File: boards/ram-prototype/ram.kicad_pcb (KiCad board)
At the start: 4 copper layers, 158 x 90 mm, 391 parts, among them J1 PinHeader_1x16_P2.54mm_Vertic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, U1 DSBGA\-5_NumericPads, U10 DSBGA\-5_NumericPads, U100 DSBGA\-5_NumericPads, U101 DSBGA\-5_NumericPads, U102 DSBGA\-5_NumericPads, U103 DSBGA\-5_NumericPads, U104 DSBGA\-5_NumericPads, U105 DSBGA\-5_NumericPads, U106 DSBGA\-5_NumericPads, U107 DSBGA\-5_NumericPads, U108 DSBGA\-5_NumericPads, U109 DSBGA\-5_NumericPads, U11 DSBGA\-5_NumericPads, U110 DSBGA\-5_NumericPads, U111 DSBGA\-5_NumericPads, U112 DSBGA\-5_NumericPads, U113 DSBGA\-5_NumericPads, U114 DSBGA\-5_NumericPads, U115 DSBGA\-5_NumericPads, U116 DSBGA\-5_NumericPads, U117 DSBGA\-5_NumericPads, U118 DSBGA\-5_NumericPads, U119 DSBGA\-5_NumericPads, U12 DSBGA\-5_NumericPads, U120 DSBGA\-5_NumericPads, U121 DSBGA\-5_NumericPads, U122 DSBGA\-5_NumericPads, U123 DSBGA\-5_NumericPads, U124 DSBGA\-5_NumericPads, U125 DSBGA\-5_NumericPads, U126 DSBGA\-5_NumericPads, U127 DSBGA\-5_NumericPads, U128 DSBGA\-5_NumericPads, U129 DSBGA\-5_NumericPads, U13 DSBGA\-5_NumericPads, U130 DSBGA\-5_NumericPads, U131 DSBGA\-5_NumericPads, U132 DSBGA\-5_NumericPads, U133 DSBGA\-5_NumericPads, U134 DSBGA\-5_NumericPads, U135 DSBGA\-5_NumericPads, U136 DSBGA\-5_NumericPads, U137 DSBGA\-5_NumericPads, U138 DSBGA\-5_NumericPads, U139 DSBGA\-5_NumericPads, U14 DSBGA\-5_NumericPads, U140 DSBGA\-5_NumericPads, U141 DSBGA\-5_NumericPads, U142 DSBGA\-5_NumericPads, U143 DSBGA\-5_NumericPads, U144 DSBGA\-5_NumericPads, U145 DSBGA\-5_NumericPads, U146 DSBGA\-5_NumericPads, U147 DSBGA\-5_NumericPads, U148 DSBGA\-5_NumericPads, U149 DSBGA\-5_NumericPads, U15 DSBGA\-5_NumericPads, U150 DSBGA\-5_NumericPads, U151 DSBGA\-5_NumericPads, U152 DSBGA\-5_NumericPads, U153 DSBGA\-5_NumericPads, U154 DSBGA\-5_NumericPads, U155 DSBGA\-5_NumericPads, U156 DSBGA\-5_NumericPads, U157 DSBGA\-5_NumericPads, U158 DSBGA\-5_NumericPads, U16 DSBGA\-5_NumericPads, U17 DSBGA\-5_NumericPads, U18 DSBGA\-5_NumericPads, U19 DSBGA\-5_NumericPads, U2 DSBGA\-5_NumericPads, U20 DSBGA\-5_NumericPads, U21 DSBGA\-5_NumericPads, U22 DSBGA\-5_NumericPads, U23 DSBGA\-8_NumericPads, U24 DSBGA\-8_NumericPads, U25 DSBGA\-8_NumericPads, U26 DSBGA\-8_NumericPads, U27 DSBGA\-8_NumericPads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

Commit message: Change layout
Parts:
- moved D35 48.6 mm to (73.3, 28.0)
- moved R35 48.6 mm to (73.3, 28.0)
- moved U21 48.6 mm to (70.9, 28.0)
- moved D34 46.7 mm to (73.3, 24.0)
- moved R34 46.7 mm to (73.3, 24.0)
- moved U20 46.7 mm to (70.9, 24.0)
- moved D33 45.7 mm to (73.3, 20.0)
- moved R33 45.7 mm to (73.3, 20.0)
- moved U19 45.7 mm to (70.9, 20.0)
- moved D36 40.0 mm to (73.3, 32.0)
- moved R36 40.0 mm to (73.3, 32.0)
- moved U22 40.0 mm to (70.9, 32.0)
- moved D31 39.2 mm to (62.4, 28.0)
- moved R31 39.2 mm to (62.4, 28.0)
- moved U17 39.2 mm to (60.0, 28.0)
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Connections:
- D1 pad 2: /Address Decoder/A0 -> /Control Logic/nOE
- D10 pad 2: /D3 -> /D4
- D11 pad 2: /D4 -> /D5
- D12 pad 2: /D5 -> /D6
- D13 pad 2: /D6 -> /D7
- D14 pad 2: /D7 -> /Column Select/A2
- D2 pad 2: /Address Decoder/A1 -> /Control Logic/nWE
- D3 pad 2: /Column Select/A2 -> /Control Logic/nCE
- D4 pad 2: /Control Logic/nOE -> /Address Decoder/A1
- D5 pad 2: /Control Logic/nWE -> /Address Decoder/A0
- D6 pad 2: /Control Logic/nCE -> /D0
- D7 pad 2: /D0 -> /D1
- D8 pad 2: /D1 -> /D2
- D9 pad 2: /D2 -> /D3
- J1 pad 10: /Control Logic/nCE -> /D0
- J1 pad 11: /Control Logic/nWE -> /Address Decoder/A0
- J1 pad 12: /Control Logic/nOE -> /Address Decoder/A1
- J1 pad 13: /Column Select/A2 -> /Control Logic/nCE
- J1 pad 14: /Address Decoder/A1 -> /Control Logic/nWE
- J1 pad 15: /Address Decoder/A0 -> /Control Logic/nOE
- J1 pad 2: /D7 -> /Column Select/A2
- J1 pad 3: /D6 -> /D7
- J1 pad 4: /D5 -> /D6
- J1 pad 5: /D4 -> /D5
- J1 pad 6: /D3 -> /D4
- J1 pad 7: /D2 -> /D3
- J1 pad 8: /D1 -> /D2
- J1 pad 9: /D0 -> /D1
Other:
- board size 158 x 90 mm -> 164 x 98 mm

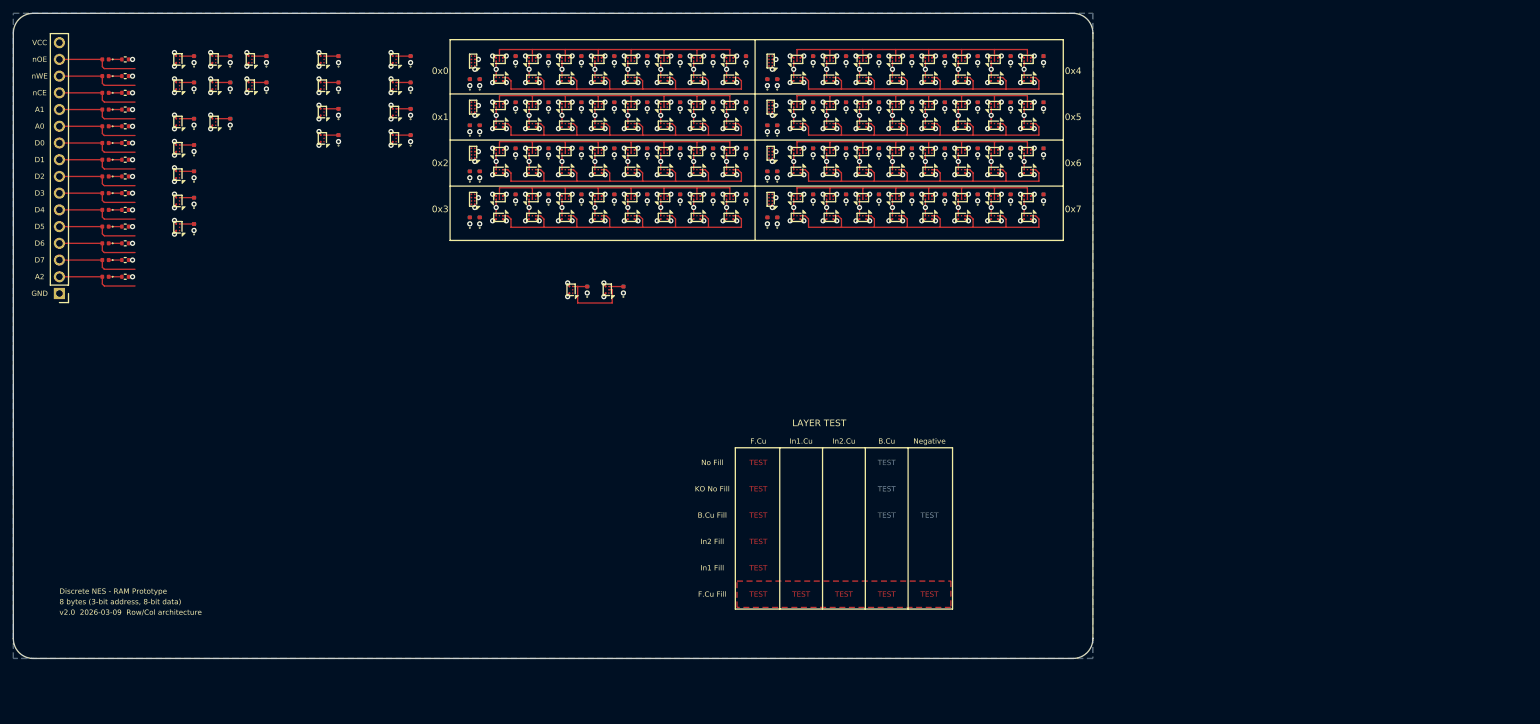
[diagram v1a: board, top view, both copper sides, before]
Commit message: clean up silkscreen
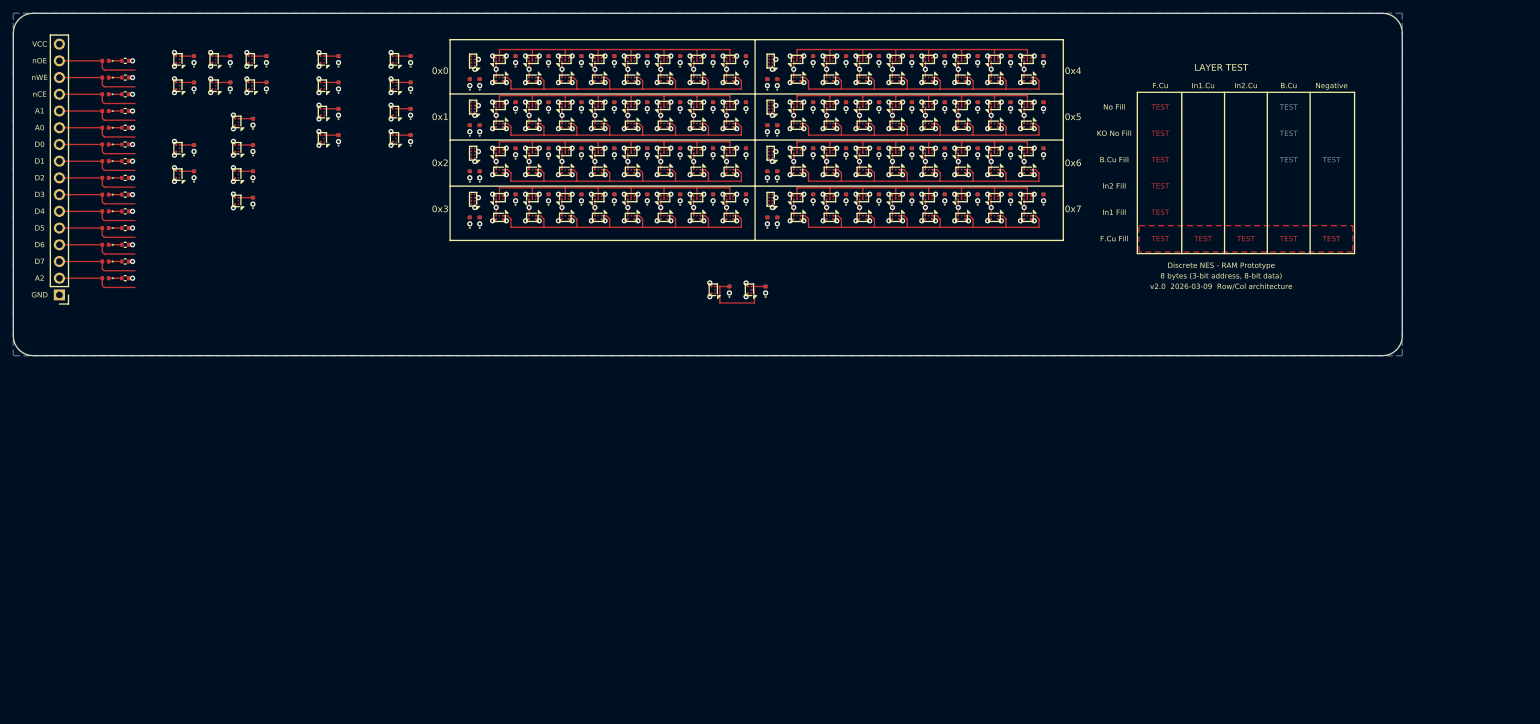
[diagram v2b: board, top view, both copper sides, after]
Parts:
- moved D21 21.6 mm to (121.8, 55.0)
- moved D22 21.6 mm to (127.3, 55.0)
- moved R21 21.6 mm to (121.8, 55.0)
- moved R22 21.6 mm to (127.3, 55.0)
- moved U7 21.6 mm to (119.3, 55.0)
- moved U8 21.6 mm to (124.8, 55.0)
- moved U3 9.80 mm to (47.0, 29.5)
- moved U4 9.80 mm to (47.0, 33.5)
- moved U5 9.80 mm to (47.0, 37.5)
- moved U6 9.80 mm to (47.0, 41.5)
- moved D17 9.80 mm to (49.4, 29.5)
- moved D18 9.80 mm to (49.4, 33.5)
- moved D19 9.80 mm to (49.4, 37.5)
- moved D20 9.80 mm to (49.4, 41.5)
- moved R17 9.80 mm to (49.4, 29.5)
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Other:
- board size 164 x 98 mm -> 211 x 52 mm

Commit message: refactor read and write schematics into row control sheets
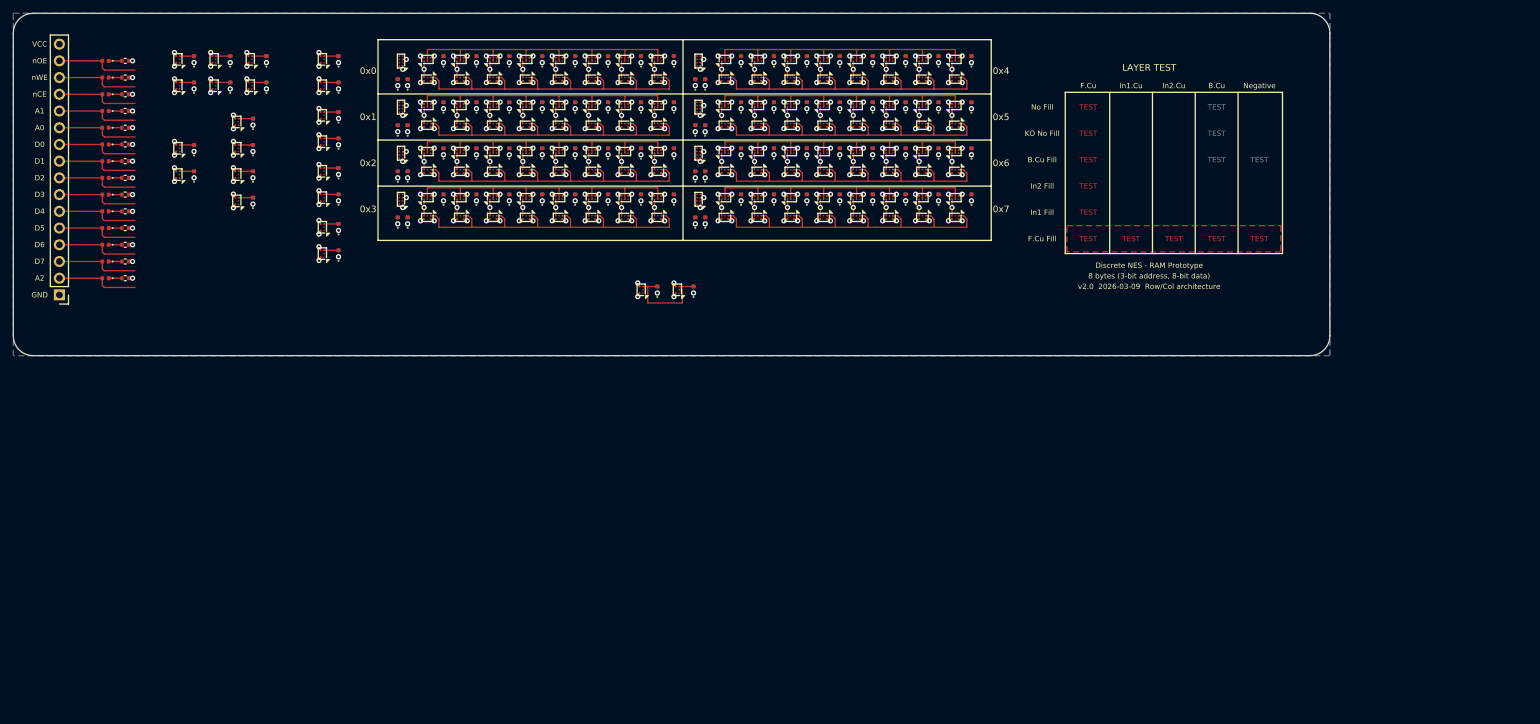
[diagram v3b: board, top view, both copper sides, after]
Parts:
- moved U22 20.6 mm to (60.0, 49.5)
- moved D36 20.6 mm to (62.4, 49.5)
- moved R36 20.6 mm to (62.4, 49.5)
- moved U21 17.0 mm to (60.0, 41.0)
- moved D35 17.0 mm to (62.4, 41.0)
- moved R35 17.0 mm to (62.4, 41.0)
- moved U20 13.9 mm to (60.0, 32.5)
- moved D34 13.9 mm to (62.4, 32.5)
- moved R34 13.9 mm to (62.4, 32.5)
- moved D32 13.5 mm to (62.4, 45.5)
- moved R32 13.5 mm to (62.4, 45.5)
- moved U18 13.5 mm to (60.0, 45.5)
- moved U19 11.7 mm to (60.0, 24.0)
- moved D33 11.7 mm to (62.4, 24.0)
- moved R33 11.7 mm to (62.4, 24.0)
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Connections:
- net /Control Logic/READ_EN renamed /READ_EN
- net /Control Logic/WRITE_ACTIVE renamed /WRITE_ACTIVE
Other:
- board size 211 x 52 mm -> 200 x 52 mm

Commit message: Add initial changes to make logic close to final
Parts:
- added D117: LED_0402_1005Metric, LED_SMD:LED_0402_1005Metric, F.Cu at (103.3, 27.0)
- added D118: LED_0402_1005Metric, LED_SMD:LED_0402_1005Metric, F.Cu at (103.3, 34.0)
- added D119: LED_0402_1005Metric, LED_SMD:LED_0402_1005Metric, F.Cu at (103.3, 41.0)
- added D120: LED_0402_1005Metric, LED_SMD:LED_0402_1005Metric, F.Cu at (148.6, 20.0)
- added D121: LED_0402_1005Metric, LED_SMD:LED_0402_1005Metric, F.Cu at (148.6, 27.0)
- added D122: LED_0402_1005Metric, LED_SMD:LED_0402_1005Metric, F.Cu at (148.6, 34.0)
- added D123: LED_0402_1005Metric, LED_SMD:LED_0402_1005Metric, F.Cu at (148.6, 41.0)
- added D124: LED_0402_1005Metric, LED_SMD:LED_0402_1005Metric, F.Cu at (98.3, 20.0)
- added D125: LED_0402_1005Metric, LED_SMD:LED_0402_1005Metric, F.Cu at (98.3, 27.0)
- added D126: LED_0402_1005Metric, LED_SMD:LED_0402_1005Metric, F.Cu at (98.3, 34.0)
- added D127: LED_0402_1005Metric, LED_SMD:LED_0402_1005Metric, F.Cu at (98.3, 41.0)
- added D128: LED_0402_1005Metric, LED_SMD:LED_0402_1005Metric, F.Cu at (143.6, 20.0)
- added D129: LED_0402_1005Metric, LED_SMD:LED_0402_1005Metric, F.Cu at (143.6, 27.0)
- added D130: LED_0402_1005Metric, LED_SMD:LED_0402_1005Metric, F.Cu at (143.6, 34.0)
- added D131: LED_0402_1005Metric, LED_SMD:LED_0402_1005Metric, F.Cu at (143.6, 41.0)
- added D132: LED_0402_1005Metric, LED_SMD:LED_0402_1005Metric, F.Cu at (93.3, 20.0)
- added D133: LED_0402_1005Metric, LED_SMD:LED_0402_1005Metric, F.Cu at (93.3, 27.0)
- added D134: LED_0402_1005Metric, LED_SMD:LED_0402_1005Metric, F.Cu at (93.3, 34.0)
- added D135: LED_0402_1005Metric, LED_SMD:LED_0402_1005Metric, F.Cu at (93.3, 41.0)
- added D136: LED_0402_1005Metric, LED_SMD:LED_0402_1005Metric, F.Cu at (138.6, 20.0)
- added D137: LED_0402_1005Metric, LED_SMD:LED_0402_1005Metric, F.Cu at (138.6, 27.0)
- added D138: LED_0402_1005Metric, LED_SMD:LED_0402_1005Metric, F.Cu at (138.6, 34.0)
- added D139: LED_0402_1005Metric, LED_SMD:LED_0402_1005Metric, F.Cu at (138.6, 41.0)
- added D140: LED_0402_1005Metric, LED_SMD:LED_0402_1005Metric, F.Cu at (88.3, 20.0)
- added D141: LED_0402_1005Metric, LED_SMD:LED_0402_1005Metric, F.Cu at (88.3, 27.0)
- added D142: LED_0402_1005Metric, LED_SMD:LED_0402_1005Metric, F.Cu at (88.3, 34.0)
- added D143: LED_0402_1005Metric, LED_SMD:LED_0402_1005Metric, F.Cu at (88.3, 41.0)
- added D144: LED_0402_1005Metric, LED_SMD:LED_0402_1005Metric, F.Cu at (133.6, 20.0)
- added D145: LED_0402_1005Metric, LED_SMD:LED_0402_1005Metric, F.Cu at (133.6, 27.0)
- added D146: LED_0402_1005Metric, LED_SMD:LED_0402_1005Metric, F.Cu at (133.6, 34.0)
- added D147: LED_0402_1005Metric, LED_SMD:LED_0402_1005Metric, F.Cu at (133.6, 41.0)
- added D148: LED_0402_1005Metric, LED_SMD:LED_0402_1005Metric, F.Cu at (83.3, 20.0)
- added D149: LED_0402_1005Metric, LED_SMD:LED_0402_1005Metric, F.Cu at (83.3, 27.0)
- added D150: LED_0402_1005Metric, LED_SMD:LED_0402_1005Metric, F.Cu at (83.3, 34.0)
- added D151: LED_0402_1005Metric, LED_SMD:LED_0402_1005Metric, F.Cu at (83.3, 41.0)
- added D152: LED_0402_1005Metric, LED_SMD:LED_0402_1005Metric, F.Cu at (128.6, 20.0)
- added D153: LED_0402_1005Metric, LED_SMD:LED_0402_1005Metric, F.Cu at (128.6, 27.0)
- added D154: LED_0402_1005Metric, LED_SMD:LED_0402_1005Metric, F.Cu at (128.6, 34.0)
- added D155: LED_0402_1005Metric, LED_SMD:LED_0402_1005Metric, F.Cu at (128.6, 41.0)
- added D156: LED_0402_1005Metric, LED_SMD:LED_0402_1005Metric, F.Cu at (78.3, 20.0)
- added D157: LED_0402_1005Metric, LED_SMD:LED_0402_1005Metric, F.Cu at (78.3, 27.0)
- added D158: LED_0402_1005Metric, LED_SMD:LED_0402_1005Metric, F.Cu at (78.3, 34.0)
- added D159: LED_0402_1005Metric, LED_SMD:LED_0402_1005Metric, F.Cu at (78.3, 41.0)
- added D160: LED_0402_1005Metric, LED_SMD:LED_0402_1005Metric, F.Cu at (123.5, 20.0)
- added D161: LED_0402_1005Metric, LED_SMD:LED_0402_1005Metric, F.Cu at (123.5, 27.0)
- added D162: LED_0402_1005Metric, LED_SMD:LED_0402_1005Metric, F.Cu at (123.5, 34.0)
- added D163: LED_0402_1005Metric, LED_SMD:LED_0402_1005Metric, F.Cu at (123.5, 41.0)
- added J2: PinHeader_1x12_P2.54mm_Vertical, Connector_PinHeader_2.54mm:PinHeader_1x12_P2.54mm_Vertical, B.Cu at (38.0, 80.0)
- added J3: PinHeader_1x14_P2.54mm_Vertical, Connector_PinHeader_2.54mm:PinHeader_1x14_P2.54mm_Vertical, B.Cu at (165.3, 54.0)
- added R117: R_0402_1005Metric, Resistor_SMD:R_0402_1005Metric, B.Cu at (103.3, 27.0)
- added R118: R_0402_1005Metric, Resistor_SMD:R_0402_1005Metric, B.Cu at (103.3, 34.0)
- added R119: R_0402_1005Metric, Resistor_SMD:R_0402_1005Metric, B.Cu at (103.3, 41.0)
- added R120: R_0402_1005Metric, Resistor_SMD:R_0402_1005Metric, B.Cu at (148.6, 20.0)
- added R121: R_0402_1005Metric, Resistor_SMD:R_0402_1005Metric, B.Cu at (148.6, 27.0)
- added R122: R_0402_1005Metric, Resistor_SMD:R_0402_1005Metric, B.Cu at (148.6, 34.0)
- added R123: R_0402_1005Metric, Resistor_SMD:R_0402_1005Metric, B.Cu at (148.6, 41.0)
- added R124: R_0402_1005Metric, Resistor_SMD:R_0402_1005Metric, B.Cu at (98.3, 20.0)
- added R125: R_0402_1005Metric, Resistor_SMD:R_0402_1005Metric, B.Cu at (98.3, 27.0)
- added R126: R_0402_1005Metric, Resistor_SMD:R_0402_1005Metric, B.Cu at (98.3, 34.0)
- added R127: R_0402_1005Metric, Resistor_SMD:R_0402_1005Metric, B.Cu at (98.3, 41.0)
- added R128: R_0402_1005Metric, Resistor_SMD:R_0402_1005Metric, B.Cu at (143.6, 20.0)
- added R129: R_0402_1005Metric, Resistor_SMD:R_0402_1005Metric, B.Cu at (143.6, 27.0)
- added R130: R_0402_1005Metric, Resistor_SMD:R_0402_1005Metric, B.Cu at (143.6, 34.0)
- added R131: R_0402_1005Metric, Resistor_SMD:R_0402_1005Metric, B.Cu at (143.6, 41.0)
- added R132: R_0402_1005Metric, Resistor_SMD:R_0402_1005Metric, B.Cu at (93.3, 20.0)
- added R133: R_0402_1005Metric, Resistor_SMD:R_0402_1005Metric, B.Cu at (93.3, 27.0)
- added R134: R_0402_1005Metric, Resistor_SMD:R_0402_1005Metric, B.Cu at (93.3, 34.0)
- added R135: R_0402_1005Metric, Resistor_SMD:R_0402_1005Metric, B.Cu at (93.3, 41.0)
- added R136: R_0402_1005Metric, Resistor_SMD:R_0402_1005Metric, B.Cu at (138.6, 20.0)
- added R137: R_0402_1005Metric, Resistor_SMD:R_0402_1005Metric, B.Cu at (138.6, 27.0)
- added R138: R_0402_1005Metric, Resistor_SMD:R_0402_1005Metric, B.Cu at (138.6, 34.0)
- added R139: R_0402_1005Metric, Resistor_SMD:R_0402_1005Metric, B.Cu at (138.6, 41.0)
- added R140: R_0402_1005Metric, Resistor_SMD:R_0402_1005Metric, B.Cu at (88.3, 20.0)
- added R141: R_0402_1005Metric, Resistor_SMD:R_0402_1005Metric, B.Cu at (88.3, 27.0)
- added R142: R_0402_1005Metric, Resistor_SMD:R_0402_1005Metric, B.Cu at (88.3, 34.0)
- added R143: R_0402_1005Metric, Resistor_SMD:R_0402_1005Metric, B.Cu at (88.3, 41.0)
- added R144: R_0402_1005Metric, Resistor_SMD:R_0402_1005Metric, B.Cu at (133.6, 20.0)
- added R145: R_0402_1005Metric, Resistor_SMD:R_0402_1005Metric, B.Cu at (133.6, 27.0)
- added R146: R_0402_1005Metric, Resistor_SMD:R_0402_1005Metric, B.Cu at (133.6, 34.0)
- added R147: R_0402_1005Metric, Resistor_SMD:R_0402_1005Metric, B.Cu at (133.6, 41.0)
- added R148: R_0402_1005Metric, Resistor_SMD:R_0402_1005Metric, B.Cu at (83.3, 20.0)
- added R149: R_0402_1005Metric, Resistor_SMD:R_0402_1005Metric, B.Cu at (83.3, 27.0)
- added R150: R_0402_1005Metric, Resistor_SMD:R_0402_1005Metric, B.Cu at (83.3, 34.0)
- added R151: R_0402_1005Metric, Resistor_SMD:R_0402_1005Metric, B.Cu at (83.3, 41.0)
- added R152: R_0402_1005Metric, Resistor_SMD:R_0402_1005Metric, B.Cu at (128.6, 20.0)
- added R153: R_0402_1005Metric, Resistor_SMD:R_0402_1005Metric, B.Cu at (128.6, 27.0)
- added R154: R_0402_1005Metric, Resistor_SMD:R_0402_1005Metric, B.Cu at (128.6, 34.0)
- added R155: R_0402_1005Metric, Resistor_SMD:R_0402_1005Metric, B.Cu at (128.6, 41.0)
- added R156: R_0402_1005Metric, Resistor_SMD:R_0402_1005Metric, B.Cu at (78.3, 20.0)
- added R157: R_0402_1005Metric, Resistor_SMD:R_0402_1005Metric, B.Cu at (78.3, 27.0)
- added R158: R_0402_1005Metric, Resistor_SMD:R_0402_1005Metric, B.Cu at (78.3, 34.0)
- added R159: R_0402_1005Metric, Resistor_SMD:R_0402_1005Metric, B.Cu at (78.3, 41.0)
- added R160: R_0402_1005Metric, Resistor_SMD:R_0402_1005Metric, B.Cu at (123.5, 20.0)
- added R161: R_0402_1005Metric, Resistor_SMD:R_0402_1005Metric, B.Cu at (123.5, 27.0)
- added R162: R_0402_1005Metric, Resistor_SMD:R_0402_1005Metric, B.Cu at (123.5, 34.0)
- added R163: R_0402_1005Metric, Resistor_SMD:R_0402_1005Metric, B.Cu at (123.5, 41.0)
- added U159: DSBGA\-5_NumericPads, DSBGA_Packages:DSBGA-5_NumericPads, F.Cu at (85.9, 30.0)
- added U160: DSBGA\-5_NumericPads, DSBGA_Packages:DSBGA-5_NumericPads, F.Cu at (85.9, 37.0)
- added U161: DSBGA\-5_NumericPads, DSBGA_Packages:DSBGA-5_NumericPads, F.Cu at (85.9, 44.0)
- added U162: DSBGA\-5_NumericPads, DSBGA_Packages:DSBGA-5_NumericPads, F.Cu at (131.1, 23.0)
- added U163: DSBGA\-5_NumericPads, DSBGA_Packages:DSBGA-5_NumericPads, F.Cu at (131.1, 30.0)
- added U164: DSBGA\-5_NumericPads, DSBGA_Packages:DSBGA-5_NumericPads, F.Cu at (131.1, 37.0)
- added U165: DSBGA\-5_NumericPads, DSBGA_Packages:DSBGA-5_NumericPads, F.Cu at (131.1, 44.0)
- added U166: DSBGA\-5_NumericPads, DSBGA_Packages:DSBGA-5_NumericPads, F.Cu at (80.9, 20.0)
- added U167: DSBGA\-5_NumericPads, DSBGA_Packages:DSBGA-5_NumericPads, F.Cu at (80.9, 27.0)
- added U168: DSBGA\-5_NumericPads, DSBGA_Packages:DSBGA-5_NumericPads, F.Cu at (80.9, 34.0)
- added U169: DSBGA\-5_NumericPads, DSBGA_Packages:DSBGA-5_NumericPads, F.Cu at (80.9, 41.0)
- added U170: DSBGA\-5_NumericPads, DSBGA_Packages:DSBGA-5_NumericPads, F.Cu at (126.1, 20.0)
- added U171: DSBGA\-5_NumericPads, DSBGA_Packages:DSBGA-5_NumericPads, F.Cu at (126.1, 27.0)
- added U172: DSBGA\-5_NumericPads, DSBGA_Packages:DSBGA-5_NumericPads, F.Cu at (126.1, 34.0)
- added U173: DSBGA\-5_NumericPads, DSBGA_Packages:DSBGA-5_NumericPads, F.Cu at (126.1, 41.0)
- added U174: DSBGA\-5_NumericPads, DSBGA_Packages:DSBGA-5_NumericPads, F.Cu at (80.9, 23.0)
- added U175: DSBGA\-5_NumericPads, DSBGA_Packages:DSBGA-5_NumericPads, F.Cu at (80.9, 30.0)
- added U176: DSBGA\-5_NumericPads, DSBGA_Packages:DSBGA-5_NumericPads, F.Cu at (80.9, 37.0)
- added U177: DSBGA\-5_NumericPads, DSBGA_Packages:DSBGA-5_NumericPads, F.Cu at (80.9, 44.0)
- added U178: DSBGA\-5_NumericPads, DSBGA_Packages:DSBGA-5_NumericPads, F.Cu at (126.1, 23.0)
- added U179: DSBGA\-5_NumericPads, DSBGA_Packages:DSBGA-5_NumericPads, F.Cu at (126.1, 30.0)
- added U180: DSBGA\-5_NumericPads, DSBGA_Packages:DSBGA-5_NumericPads, F.Cu at (126.1, 37.0)
- added U181: DSBGA\-5_NumericPads, DSBGA_Packages:DSBGA-5_NumericPads, F.Cu at (126.1, 44.0)
- added U182: DSBGA\-5_NumericPads, DSBGA_Packages:DSBGA-5_NumericPads, F.Cu at (75.9, 20.0)
- added U183: DSBGA\-5_NumericPads, DSBGA_Packages:DSBGA-5_NumericPads, F.Cu at (75.9, 27.0)
- added U184: DSBGA\-5_NumericPads, DSBGA_Packages:DSBGA-5_NumericPads, F.Cu at (75.9, 34.0)
- added U185: DSBGA\-5_NumericPads, DSBGA_Packages:DSBGA-5_NumericPads, F.Cu at (75.9, 41.0)
- added U186: DSBGA\-5_NumericPads, DSBGA_Packages:DSBGA-5_NumericPads, F.Cu at (121.1, 20.0)
- added U187: DSBGA\-5_NumericPads, DSBGA_Packages:DSBGA-5_NumericPads, F.Cu at (121.1, 27.0)
- added U188: DSBGA\-5_NumericPads, DSBGA_Packages:DSBGA-5_NumericPads, F.Cu at (121.1, 34.0)
- added U189: DSBGA\-5_NumericPads, DSBGA_Packages:DSBGA-5_NumericPads, F.Cu at (121.1, 41.0)
- added U190: DSBGA\-5_NumericPads, DSBGA_Packages:DSBGA-5_NumericPads, F.Cu at (75.9, 23.0)
- added U191: DSBGA\-5_NumericPads, DSBGA_Packages:DSBGA-5_NumericPads, F.Cu at (75.9, 30.0)
- added U192: DSBGA\-5_NumericPads, DSBGA_Packages:DSBGA-5_NumericPads, F.Cu at (75.9, 37.0)
- added U193: DSBGA\-5_NumericPads, DSBGA_Packages:DSBGA-5_NumericPads, F.Cu at (75.9, 44.0)
- added U194: DSBGA\-5_NumericPads, DSBGA_Packages:DSBGA-5_NumericPads, F.Cu at (121.1, 23.0)
- added U195: DSBGA\-5_NumericPads, DSBGA_Packages:DSBGA-5_NumericPads, F.Cu at (121.1, 30.0)
- added U196: DSBGA\-5_NumericPads, DSBGA_Packages:DSBGA-5_NumericPads, F.Cu at (121.1, 37.0)
- added U197: DSBGA\-5_NumericPads, DSBGA_Packages:DSBGA-5_NumericPads, F.Cu at (121.1, 44.0)
- J1: value PinHeader_1x16_P2.54mm_Vertical -> PinHeader_1x24_P2.54mm_Vertical; footprint Connector_PinHeader_2.54mm:PinHeader_1x16_P2.54mm_Vertical -> Connector_PinHeader_2.54mm:PinHeader_1x24_P2.54mm_Vertical
- R1, R10, R11, R12, R13, R14, R2, R3, R4, R5, R6, R7, R8, R9: moved to B.Cu
- U23, U24, U25, U26, U27, U28, U29, U30: value DSBGA\-8_NumericPads -> DSBGA\-5_NumericPads; footprint DSBGA_Packages:DSBGA-8_NumericPads -> DSBGA_Packages:DSBGA-5_NumericPads
- U62, U63, U64, U65, U66, U67, U68, U69: value DSBGA\-5_NumericPads -> DSBGA\-8_NumericPads; footprint DSBGA_Packages:DSBGA-5_NumericPads -> DSBGA_Packages:DSBGA-8_NumericPads
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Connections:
- D10 pad 2: /D4 -> /Address Decoder/A0
- D11 pad 2: /D5 -> /D0
- D12 pad 2: /D6 -> /D1
- D13 pad 2: /D7 -> /D2
- D14 pad 2: /Column Select/A2 -> /D3
- D15 pad 2: Net-(D15-A) -> /D4
- D16 pad 2: Net-(D16-A) -> /D5
- D17 pad 2: /Address Decoder/ROW_SEL_0 -> /D6
- D18 pad 2: /Address Decoder/ROW_SEL_1 -> /D7
- D19 pad 2: /Address Decoder/ROW_SEL_2 -> /Column Select/A10
- D20 pad 2: /Address Decoder/ROW_SEL_3 -> /Column Select/A9
- D21 pad 2: /COL_SEL_0 -> /Column Select/A8
- D22 pad 2: /COL_SEL_1 -> /Column Select/A7
- D27 pad 2: /WRITE_ACTIVE -> Net-(D27-A)
- D28 pad 2: /READ_EN -> Net-(D28-A)
- D29 pad 2: /WRITE_EN_ROW_0 -> Net-(D29-A)
- D30 pad 2: /WRITE_EN_ROW_1 -> /RS1
- D31 pad 2: /WRITE_EN_ROW_2 -> /RS2
- D32 pad 2: /WRITE_EN_ROW_3 -> /RS3
- D33 pad 2: /READ_EN_ROW_0 -> /RS4
- D34 pad 2: /READ_EN_ROW_1 -> Net-(D34-A)
- D35 pad 2: /READ_EN_ROW_2 -> Net-(D35-A)
- D36 pad 2: /READ_EN_ROW_3 -> Net-(D36-A)
- D38 pad 2: Net-(D38-A) -> /Address Decoder/ROW_SEL_0
- D39 pad 2: Net-(D39-A) -> /Address Decoder/ROW_SEL_1
- D4 pad 2: /Address Decoder/A1 -> /Address Decoder/A6
- D40 pad 2: Net-(D40-A) -> /Address Decoder/ROW_SEL_2
- D41 pad 2: Net-(D41-A) -> /Address Decoder/ROW_SEL_3
- D46 pad 2: Net-(D46-A) -> /GA0
- D47 pad 2: Net-(D47-A) -> /GA1
- D48 pad 2: Net-(D48-A) -> /GA2
- D49 pad 2: Net-(D49-A) -> /GA3
- D5 pad 2: /Address Decoder/A0 -> /Address Decoder/A5
- D50 pad 2: Net-(D50-A) -> /GB0
- D51 pad 2: Net-(D51-A) -> /GB1
- D52 pad 2: Net-(D52-A) -> /GB2
- D53 pad 2: Net-(D53-A) -> /GB3
- D54 pad 2: Net-(D54-A) -> /COL_SEL_0
- D55 pad 2: Net-(D55-A) -> /COL_SEL_1
- D56 pad 2: Net-(D56-A) -> /COL_SEL_2
- D57 pad 2: Net-(D57-A) -> /COL_SEL_3
- D58 pad 2: Net-(D58-A) -> /COL_SEL_4
- D59 pad 2: Net-(D59-A) -> /COL_SEL_5
- D6 pad 2: /D0 -> /Address Decoder/A4
- D60 pad 2: Net-(D60-A) -> /COL_SEL_6
- D61 pad 2: Net-(D61-A) -> /COL_SEL_7
- D62 pad 2: Net-(D62-A) -> /COL_SEL_8
- D63 pad 2: Net-(D63-A) -> /COL_SEL_9
- D64 pad 2: Net-(D64-A) -> /COL_SEL_10
- D65 pad 2: Net-(D65-A) -> /COL_SEL_11
- D66 pad 2: Net-(D66-A) -> /COL_SEL_12
- D67 pad 2: Net-(D67-A) -> /COL_SEL_13
- D68 pad 2: Net-(D68-A) -> /COL_SEL_14
- D69 pad 2: Net-(D69-A) -> /COL_SEL_15
- D7 pad 2: /D1 -> /Address Decoder/A3
- D74 pad 2: Net-(D74-A) -> /WRITE_ACTIVE
- D75 pad 2: Net-(D75-A) -> /READ_EN
- D76 pad 2: Net-(D76-A) -> /WRITE_EN_ROW_0
- D77 pad 2: Net-(D77-A) -> /WRITE_EN_ROW_1
- D78 pad 2: Net-(D78-A) -> /WRITE_EN_ROW_2
- D79 pad 2: Net-(D79-A) -> /WRITE_EN_ROW_3
- D8 pad 2: /D2 -> /Address Decoder/A2
- D80 pad 2: Net-(D80-A) -> /READ_EN_ROW_0
- D81 pad 2: Net-(D81-A) -> /READ_EN_ROW_1
- D82 pad 2: Net-(D82-A) -> /READ_EN_ROW_2
- D83 pad 2: Net-(D83-A) -> /READ_EN_ROW_3
- D9 pad 2: /D3 -> /Address Decoder/A1
- J1 pad 10: /D0 -> /D3
- J1 pad 11: /Address Decoder/A0 -> /D2
- J1 pad 12: /Address Decoder/A1 -> /D1
- J1 pad 13: /Control Logic/nCE -> /D0
- J1 pad 14: /Control Logic/nWE -> /Address Decoder/A0
- J1 pad 15: /Control Logic/nOE -> /Address Decoder/A1
- J1 pad 16: VCC -> /Address Decoder/A2
- J1 pad 2: /Column Select/A2 -> /Column Select/A7
- J1 pad 3: /D7 -> /Column Select/A8
- J1 pad 4: /D6 -> /Column Select/A9
- J1 pad 5: /D5 -> /Column Select/A10
- J1 pad 6: /D4 -> /D7
- J1 pad 7: /D3 -> /D6
- J1 pad 8: /D2 -> /D5
- J1 pad 9: /D1 -> /D4
- U1 pad 4: Net-(D15-A) -> Net-(D23-A)
- U10 pad 1: (no net) -> /RS1
- U10 pad 2: /Control Logic/nOE -> /RS2
- U10 pad 4: Net-(D24-A) -> /RS3
- U100 pad 1: /D4 -> Net-(D98-A)
- U100 pad 2: Net-(D42-A) -> Net-(D114-A)
- U100 pad 4: Net-(D90-A) -> /D1
- U101 pad 1: /D4 -> Net-(D99-A)
- U101 pad 2: Net-(D43-A) -> Net-(D115-A)
- U101 pad 4: Net-(D91-A) -> /D1
- U102 pad 1: /D4 -> /D2
- U102 pad 2: Net-(D44-A) -> Net-(D84-A)
- U102 pad 4: Net-(D92-A) -> Net-(D116-A)
- U103 pad 1: Net-(D45-A) -> /D2
- U103 pad 4: /D4 -> Net-(D117-A)
- U104 pad 1: Net-(D46-A) -> /D2
- U104 pad 4: /D4 -> Net-(D118-A)
- U105 pad 1: Net-(D47-A) -> /D2
- U105 pad 4: /D4 -> Net-(D119-A)
- U106 pad 1: Net-(D48-A) -> /D2
- U106 pad 4: /D4 -> Net-(D120-A)
- U107 pad 1: Net-(D49-A) -> /D2
- U107 pad 4: /D4 -> Net-(D121-A)
- U108 pad 1: Net-(D50-A) -> /D2
- U108 pad 4: /D4 -> Net-(D122-A)
- U109 pad 1: Net-(D51-A) -> /D2
- U109 pad 4: /D4 -> Net-(D123-A)
- U11 pad 1: (no net) -> /RS3
- U11 pad 2: /Control Logic/nWE -> Net-(D29-A)
- U11 pad 4: Net-(D25-A) -> /RS4
- U110 pad 1: Net-(D52-A) -> Net-(D92-A)
- U110 pad 2: Net-(D92-A) -> Net-(D116-A)
- U110 pad 4: /D4 -> /D2
- U111 pad 1: /D5 -> Net-(D93-A)
- U111 pad 2: Net-(D37-A) -> Net-(D117-A)
- U111 pad 4: Net-(D93-A) -> /D2
- U112 pad 1: /D5 -> Net-(D94-A)
- U112 pad 2: Net-(D38-A) -> Net-(D118-A)
- U112 pad 4: Net-(D94-A) -> /D2
- U113 pad 1: /D5 -> Net-(D95-A)
- U113 pad 2: Net-(D39-A) -> Net-(D119-A)
- U113 pad 4: Net-(D95-A) -> /D2
- U114 pad 1: /D5 -> Net-(D96-A)
- U114 pad 2: Net-(D40-A) -> Net-(D120-A)
- U114 pad 4: Net-(D96-A) -> /D2
- U115 pad 1: /D5 -> Net-(D97-A)
- U115 pad 2: Net-(D41-A) -> Net-(D121-A)
- U115 pad 4: Net-(D97-A) -> /D2
- U116 pad 1: /D5 -> Net-(D98-A)
- U116 pad 2: Net-(D42-A) -> Net-(D122-A)
- U116 pad 4: Net-(D98-A) -> /D2
- U117 pad 1: /D5 -> Net-(D99-A)
- U117 pad 2: Net-(D43-A) -> Net-(D123-A)
- U117 pad 4: Net-(D99-A) -> /D2
- U118 pad 1: /D5 -> /D3
- U118 pad 2: Net-(D44-A) -> Net-(D84-A)
- U118 pad 4: Net-(D100-A) -> Net-(D124-A)
- U119 pad 1: Net-(D45-A) -> /D3
- U119 pad 2: Net-(D93-A) -> Net-(D85-A)
- U119 pad 4: /D5 -> Net-(D125-A)
- U12 pad 1: Net-(D23-A) -> Net-(D24-A)
- U12 pad 2: Net-(D25-A) -> Net-(D23-A)
- U12 pad 4: /WRITE_ACTIVE -> Net-(D34-A)
- U120 pad 1: Net-(D46-A) -> /D3
- U120 pad 2: Net-(D94-A) -> Net-(D86-A)
- U120 pad 4: /D5 -> Net-(D126-A)
- U121 pad 1: Net-(D47-A) -> /D3
- U121 pad 2: Net-(D95-A) -> Net-(D87-A)
- U121 pad 4: /D5 -> Net-(D127-A)
- U122 pad 1: Net-(D48-A) -> /D3
- U122 pad 2: Net-(D96-A) -> Net-(D88-A)
- U122 pad 4: /D5 -> Net-(D128-A)
- U123 pad 1: Net-(D49-A) -> /D3
- U123 pad 2: Net-(D97-A) -> Net-(D89-A)
- U123 pad 4: /D5 -> Net-(D129-A)
- U124 pad 1: Net-(D50-A) -> /D3
- U124 pad 2: Net-(D98-A) -> Net-(D90-A)
- U124 pad 4: /D5 -> Net-(D130-A)
- U125 pad 1: Net-(D51-A) -> /D3
- U125 pad 2: Net-(D99-A) -> Net-(D91-A)
- U125 pad 4: /D5 -> Net-(D131-A)
- U126 pad 1: Net-(D52-A) -> Net-(D92-A)
- U126 pad 2: Net-(D100-A) -> Net-(D124-A)
- U126 pad 4: /D5 -> /D3
- U127 pad 1: /D6 -> Net-(D93-A)
- U127 pad 2: Net-(D37-A) -> Net-(D125-A)
- U127 pad 4: Net-(D101-A) -> /D3
- U128 pad 1: /D6 -> Net-(D94-A)
- U128 pad 2: Net-(D38-A) -> Net-(D126-A)
- U128 pad 4: Net-(D102-A) -> /D3
- U129 pad 1: /D6 -> Net-(D95-A)
- U129 pad 2: Net-(D39-A) -> Net-(D127-A)
- U129 pad 4: Net-(D103-A) -> /D3
- U13 pad 1: Net-(D23-A) -> Net-(D24-A)
- U13 pad 2: Net-(D24-A) -> /Address Decoder/A0
- U13 pad 4: Net-(D26-A) -> Net-(D35-A)
- U130 pad 1: /D6 -> Net-(D96-A)
- U130 pad 2: Net-(D40-A) -> Net-(D128-A)
- U130 pad 4: Net-(D104-A) -> /D3
- U131 pad 1: /D6 -> Net-(D97-A)
- U131 pad 2: Net-(D41-A) -> Net-(D129-A)
- U131 pad 4: Net-(D105-A) -> /D3
- U132 pad 1: /D6 -> Net-(D98-A)
- U132 pad 2: Net-(D42-A) -> Net-(D130-A)
- U132 pad 4: Net-(D106-A) -> /D3
- U133 pad 1: /D6 -> Net-(D99-A)
- U133 pad 2: Net-(D43-A) -> Net-(D131-A)
- U133 pad 4: Net-(D107-A) -> /D3
- U134 pad 1: /D6 -> /D4
- U134 pad 2: Net-(D44-A) -> Net-(D84-A)
- U134 pad 4: Net-(D108-A) -> Net-(D132-A)
- U135 pad 1: Net-(D45-A) -> /D4
- U135 pad 2: Net-(D101-A) -> Net-(D85-A)
- U135 pad 4: /D6 -> Net-(D133-A)
- U136 pad 1: Net-(D46-A) -> /D4
- U136 pad 2: Net-(D102-A) -> Net-(D86-A)
- U136 pad 4: /D6 -> Net-(D134-A)
- U137 pad 1: Net-(D47-A) -> /D4
- U137 pad 2: Net-(D103-A) -> Net-(D87-A)
- U137 pad 4: /D6 -> Net-(D135-A)
- U138 pad 1: Net-(D48-A) -> /D4
- U138 pad 2: Net-(D104-A) -> Net-(D88-A)
- U138 pad 4: /D6 -> Net-(D136-A)
- U139 pad 1: Net-(D49-A) -> /D4
- U139 pad 2: Net-(D105-A) -> Net-(D89-A)
- U139 pad 4: /D6 -> Net-(D137-A)
- U14 pad 1: Net-(D26-A) -> /Address Decoder/A1
- U14 pad 2: /Control Logic/nWE -> Net-(D23-A)
- U14 pad 4: /READ_EN -> Net-(D36-A)
- U140 pad 1: Net-(D50-A) -> /D4
- U140 pad 2: Net-(D106-A) -> Net-(D90-A)
- U140 pad 4: /D6 -> Net-(D138-A)
- U141 pad 1: Net-(D51-A) -> /D4
- U141 pad 2: Net-(D107-A) -> Net-(D91-A)
- U141 pad 4: /D6 -> Net-(D139-A)
- U142 pad 1: Net-(D52-A) -> Net-(D92-A)
- U142 pad 2: Net-(D108-A) -> Net-(D132-A)
- U142 pad 4: /D6 -> /D4
- U143 pad 1: /D7 -> Net-(D93-A)
- U143 pad 2: Net-(D37-A) -> Net-(D133-A)
- U143 pad 4: Net-(D109-A) -> /D4
- U144 pad 1: /D7 -> Net-(D94-A)
- U144 pad 2: Net-(D38-A) -> Net-(D134-A)
- U144 pad 4: Net-(D110-A) -> /D4
- U145 pad 1: /D7 -> Net-(D95-A)
- U145 pad 2: Net-(D39-A) -> Net-(D135-A)
- U145 pad 4: Net-(D111-A) -> /D4
- U146 pad 1: /D7 -> Net-(D96-A)
- U146 pad 2: Net-(D40-A) -> Net-(D136-A)
- U146 pad 4: Net-(D112-A) -> /D4
- U147 pad 1: /D7 -> Net-(D97-A)
- U147 pad 2: Net-(D41-A) -> Net-(D137-A)
- U147 pad 4: Net-(D113-A) -> /D4
- U148 pad 1: /D7 -> Net-(D98-A)
- U148 pad 2: Net-(D42-A) -> Net-(D138-A)
- U148 pad 4: Net-(D114-A) -> /D4
- U149 pad 1: /D7 -> Net-(D99-A)
- U149 pad 2: Net-(D43-A) -> Net-(D139-A)
- U149 pad 4: Net-(D115-A) -> /D4
- U15 pad 1: /WRITE_ACTIVE -> /Address Decoder/A1
- U15 pad 2: /Address Decoder/ROW_SEL_0 -> /Address Decoder/A0
- U15 pad 4: /WRITE_EN_ROW_0 -> Net-(D37-A)
- U150 pad 1: /D7 -> /D5
- U150 pad 2: Net-(D44-A) -> Net-(D84-A)
- U150 pad 4: Net-(D116-A) -> Net-(D140-A)
- U151 pad 1: Net-(D45-A) -> /D5
- U151 pad 2: Net-(D109-A) -> Net-(D85-A)
- U151 pad 4: /D7 -> Net-(D141-A)
- U152 pad 1: Net-(D46-A) -> /D5
- U152 pad 2: Net-(D110-A) -> Net-(D86-A)
- U152 pad 4: /D7 -> Net-(D142-A)
- U153 pad 1: Net-(D47-A) -> /D5
- U153 pad 2: Net-(D111-A) -> Net-(D87-A)
- U153 pad 4: /D7 -> Net-(D143-A)
- U154 pad 1: Net-(D48-A) -> /D5
- U154 pad 2: Net-(D112-A) -> Net-(D88-A)
- U154 pad 4: /D7 -> Net-(D144-A)
- U155 pad 1: Net-(D49-A) -> /D5
- U155 pad 2: Net-(D113-A) -> Net-(D89-A)
- U155 pad 4: /D7 -> Net-(D145-A)
- U156 pad 1: Net-(D50-A) -> /D5
- U156 pad 2: Net-(D114-A) -> Net-(D90-A)
- U156 pad 4: /D7 -> Net-(D146-A)
- U157 pad 1: Net-(D51-A) -> /D5
- U157 pad 2: Net-(D115-A) -> Net-(D91-A)
- U157 pad 4: /D7 -> Net-(D147-A)
- U158 pad 1: Net-(D52-A) -> Net-(D92-A)
- U158 pad 2: Net-(D116-A) -> Net-(D140-A)
- U158 pad 4: /D7 -> /D5
- U16 pad 1: /WRITE_ACTIVE -> /RS4
- U16 pad 2: /Address Decoder/ROW_SEL_1 -> Net-(D34-A)
- U16 pad 4: /WRITE_EN_ROW_1 -> /Address Decoder/ROW_SEL_0
- U17 pad 1: /WRITE_ACTIVE -> /RS4
- U17 pad 2: /Address Decoder/ROW_SEL_2 -> Net-(D35-A)
- U17 pad 4: /WRITE_EN_ROW_2 -> /Address Decoder/ROW_SEL_1
- U18 pad 1: /WRITE_ACTIVE -> /RS4
- U18 pad 2: /Address Decoder/ROW_SEL_3 -> Net-(D36-A)
- U18 pad 4: /WRITE_EN_ROW_3 -> /Address Decoder/ROW_SEL_2
- U19 pad 1: /READ_EN -> /RS4
- U19 pad 2: /Address Decoder/ROW_SEL_0 -> Net-(D37-A)
- U19 pad 4: /READ_EN_ROW_0 -> /Address Decoder/ROW_SEL_3
- U2 pad 4: Net-(D16-A) -> Net-(D24-A)
- U20 pad 1: /READ_EN -> (no net)
- U20 pad 2: /Address Decoder/ROW_SEL_1 -> /Column Select/A7
- U20 pad 4: /READ_EN_ROW_1 -> Net-(D42-A)
- U21 pad 1: /READ_EN -> (no net)
- U21 pad 2: /Address Decoder/ROW_SEL_2 -> /Column Select/A8
- U21 pad 4: /READ_EN_ROW_2 -> Net-(D43-A)
- U22 pad 1: /READ_EN -> (no net)
- U22 pad 2: /Address Decoder/ROW_SEL_3 -> /Column Select/A9
- U22 pad 4: /READ_EN_ROW_3 -> Net-(D44-A)
- U23 pad 1: /COL_SEL_0 -> (no net)
- U23 pad 2: /WRITE_EN_ROW_0 -> /Column Select/A10
- U23 pad 3: Net-(D45-A) -> GND
- U23 pad 4: GND -> Net-(D45-A)
- U23 pad 5: /COL_SEL_0 -> VCC
- U24 pad 1: /COL_SEL_0 -> Net-(D43-A)
- U24 pad 2: /WRITE_EN_ROW_1 -> Net-(D42-A)
- U24 pad 3: Net-(D46-A) -> GND
- U24 pad 4: GND -> /GA0
- U24 pad 5: /COL_SEL_0 -> VCC
- U25 pad 1: /COL_SEL_0 -> Net-(D43-A)
- U25 pad 2: /WRITE_EN_ROW_2 -> /Column Select/A7
- U25 pad 3: Net-(D47-A) -> GND
- U25 pad 4: GND -> /GA1
- U25 pad 5: /COL_SEL_0 -> VCC
- U26 pad 1: /COL_SEL_0 -> /Column Select/A8
- U26 pad 2: /WRITE_EN_ROW_3 -> Net-(D42-A)
- U26 pad 3: Net-(D48-A) -> GND
- U26 pad 4: GND -> /GA2
- U26 pad 5: /COL_SEL_0 -> VCC
- U27 pad 1: /COL_SEL_1 -> /Column Select/A8
- U27 pad 2: /WRITE_EN_ROW_0 -> /Column Select/A7
- U27 pad 3: Net-(D49-A) -> GND
- U27 pad 4: GND -> /GA3
- U27 pad 5: /COL_SEL_1 -> VCC
- U28 pad 1: /COL_SEL_1 -> Net-(D45-A)
- U28 pad 2: /WRITE_EN_ROW_1 -> Net-(D44-A)
- U28 pad 3: Net-(D50-A) -> GND
- U28 pad 4: GND -> /GB0
- U28 pad 5: /COL_SEL_1 -> VCC
- U29 pad 1: /COL_SEL_1 -> Net-(D45-A)
- U29 pad 2: /WRITE_EN_ROW_2 -> /Column Select/A9
- U29 pad 3: Net-(D51-A) -> GND
- U29 pad 4: GND -> /GB1
- U29 pad 5: /COL_SEL_1 -> VCC
- U3 pad 1: Net-(D15-A) -> (no net)
- U3 pad 2: Net-(D16-A) -> /Address Decoder/A2
- U3 pad 4: /Address Decoder/ROW_SEL_0 -> Net-(D25-A)
- U30 pad 1: /COL_SEL_1 -> /Column Select/A10
- U30 pad 2: /WRITE_EN_ROW_3 -> Net-(D44-A)
- U30 pad 3: Net-(D52-A) -> GND
- U30 pad 4: GND -> /GB2
- U30 pad 5: /COL_SEL_1 -> VCC
- U31 pad 1: /D0 -> /Column Select/A10
- U31 pad 2: Net-(D37-A) -> /Column Select/A9
- U31 pad 4: Net-(D53-A) -> /GB3
- U32 pad 1: /D0 -> /GB0
- U32 pad 2: Net-(D38-A) -> /GA0
- U32 pad 4: Net-(D54-A) -> /COL_SEL_0
- U33 pad 1: /D0 -> /GB0
- U33 pad 2: Net-(D39-A) -> /GA1
- U33 pad 4: Net-(D55-A) -> /COL_SEL_1
- U34 pad 1: /D0 -> /GB0
- U34 pad 2: Net-(D40-A) -> /GA2
- U34 pad 4: Net-(D56-A) -> /COL_SEL_2
- U35 pad 1: /D0 -> /GB0
- U35 pad 2: Net-(D41-A) -> /GA3
- U35 pad 4: Net-(D57-A) -> /COL_SEL_3
- U36 pad 1: /D0 -> /GB1
- U36 pad 2: Net-(D42-A) -> /GA0
- U36 pad 4: Net-(D58-A) -> /COL_SEL_4
- U37 pad 1: /D0 -> /GB1
- U37 pad 2: Net-(D43-A) -> /GA1
- U37 pad 4: Net-(D59-A) -> /COL_SEL_5
- U38 pad 1: /D0 -> /GB1
- U38 pad 2: Net-(D44-A) -> /GA2
- U38 pad 4: Net-(D60-A) -> /COL_SEL_6
- U39 pad 1: Net-(D45-A) -> /GB1
- U39 pad 2: Net-(D53-A) -> /GA3
- U39 pad 4: /D0 -> /COL_SEL_7
- U4 pad 1: /Address Decoder/A0 -> (no net)
- U4 pad 2: Net-(D16-A) -> /Address Decoder/A3
- U4 pad 4: /Address Decoder/ROW_SEL_1 -> Net-(D26-A)
- U40 pad 1: Net-(D46-A) -> /GB2
- U40 pad 2: Net-(D54-A) -> /GA0
- U40 pad 4: /D0 -> /COL_SEL_8
- U41 pad 1: Net-(D47-A) -> /GB2
- U41 pad 2: Net-(D55-A) -> /GA1
- U41 pad 4: /D0 -> /COL_SEL_9
- U42 pad 1: Net-(D48-A) -> /GB2
- U42 pad 2: Net-(D56-A) -> /GA2
- U42 pad 4: /D0 -> /COL_SEL_10
- U43 pad 1: Net-(D49-A) -> /GB2
- U43 pad 2: Net-(D57-A) -> /GA3
- U43 pad 4: /D0 -> /COL_SEL_11
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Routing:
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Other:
- board size 200 x 52 mm -> 200 x 104 mm
- board text added: "8 bytes (11-bit address, 8-bit data)"
- board text added: "A10"
- board text added: "A3"
- board text added: "A4"
- board text added: "A5"
- board text added: "A6"
- board text added: "A7"
- board text added: "A8"
- board text added: "A9"
- board text added: "COL_SEL"
- board text added: "PROBE"
- board text added: "v3.0 2026-03-10 2K-depth decoders"
- board text removed: "8 bytes (3-bit address, 8-bit data)"
- board text removed: "v2.0 2026-03-09 Row/Col architecture"

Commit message: clean up
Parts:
- J2: value PinHeader_1x12_P2.54mm_Vertical -> PinHeader_1x04_P2.54mm_Vertical; footprint Connector_PinHeader_2.54mm:PinHeader_1x12_P2.54mm_Vertical -> Connector_PinHeader_2.54mm:PinHeader_1x04_P2.54mm_Vertical
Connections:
- D46 pad 2: /GA0 -> /Column Select/GA0
- D47 pad 2: /GA1 -> /Column Select/GA1
- D48 pad 2: /GA2 -> /Column Select/GA2
- D49 pad 2: /GA3 -> /Column Select/GA3
- D50 pad 2: /GB0 -> /Column Select/GB0
- D51 pad 2: /GB1 -> /Column Select/GB1
- D52 pad 2: /GB2 -> /Column Select/GB2
- D53 pad 2: /GB3 -> /Column Select/GB3
- U24 pad 4: /GA0 -> /Column Select/GA0
- U25 pad 4: /GA1 -> /Column Select/GA1
- U26 pad 4: /GA2 -> /Column Select/GA2
- U27 pad 4: /GA3 -> /Column Select/GA3
- U28 pad 4: /GB0 -> /Column Select/GB0
- U29 pad 4: /GB1 -> /Column Select/GB1
- U30 pad 4: /GB2 -> /Column Select/GB2
- U31 pad 4: /GB3 -> /Column Select/GB3
- U32 pad 1: /GB0 -> /Column Select/GB0
- U32 pad 2: /GA0 -> /Column Select/GA0
- U33 pad 1: /GB0 -> /Column Select/GB0
- U33 pad 2: /GA1 -> /Column Select/GA1
- U34 pad 1: /GB0 -> /Column Select/GB0
- U34 pad 2: /GA2 -> /Column Select/GA2
- U35 pad 1: /GB0 -> /Column Select/GB0
- U35 pad 2: /GA3 -> /Column Select/GA3
- U36 pad 1: /GB1 -> /Column Select/GB1
- U36 pad 2: /GA0 -> /Column Select/GA0
- U37 pad 1: /GB1 -> /Column Select/GB1
- U37 pad 2: /GA1 -> /Column Select/GA1
- U38 pad 1: /GB1 -> /Column Select/GB1
- U38 pad 2: /GA2 -> /Column Select/GA2
- U39 pad 1: /GB1 -> /Column Select/GB1
- U39 pad 2: /GA3 -> /Column Select/GA3
- U40 pad 1: /GB2 -> /Column Select/GB2
- U40 pad 2: /GA0 -> /Column Select/GA0
- U41 pad 1: /GB2 -> /Column Select/GB2
- U41 pad 2: /GA1 -> /Column Select/GA1
- U42 pad 1: /GB2 -> /Column Select/GB2
- U42 pad 2: /GA2 -> /Column Select/GA2
- U43 pad 1: /GB2 -> /Column Select/GB2
- U43 pad 2: /GA3 -> /Column Select/GA3
- U44 pad 1: /GB3 -> /Column Select/GB3
- U44 pad 2: /GA0 -> /Column Select/GA0
- U45 pad 1: /GB3 -> /Column Select/GB3
- U45 pad 2: /GA1 -> /Column Select/GA1
- U46 pad 1: /GB3 -> /Column Select/GB3
- U46 pad 2: /GA2 -> /Column Select/GA2
- U47 pad 1: /GB3 -> /Column Select/GB3
- U47 pad 2: /GA3 -> /Column Select/GA3
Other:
- board size 200 x 104 mm -> 200 x 84 mm
